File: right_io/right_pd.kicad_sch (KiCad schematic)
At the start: 79 parts, among them J11 USB-C dual-role data/PD port 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, J12 USB-C source-only data port J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, Q2002 2N7002K DFP USB2 enable inver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, U1760 TPS2553DDBVR 1.3A USB branch, U1761 TPS25810RVCR Type-C DFP contr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, U1763 TPD1S514-1YZR 5.9V VBUS OVP, U1765 TPD4E05U06 USB2/CC ESD, U2011 TPD4S201 CC and USB2 short-to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, U2012 CAT24C256 32KB private TPS257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, U2013 TS3USB30E DFP-qualified USB2 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, U2014 SN74LVC2G07 partial-power-dow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, U2015 TVS2200 22V USB VBUS surge cl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, U2016 SN74LVC1G08 DFP and attached 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, U2404 TPS22992SRXNR J11 PP5V gate, U2409 SN74LVC1G08DBVR J12 source pe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, U42 TPS25751AD USB-PD DRP control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, U721 TPS26630RGER PD2 default-off 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

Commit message: rework the board placement and fix more power stuff
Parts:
- added C2631: 100n 50V inverter bypass, Capacitor_SMD:C_0603_1608Metric, symbol Device:C
- added C2681: 100n 50V qualifier bypass, Capacitor_SMD:C_0603_1608Metric, symbol Device:C
- added Q2631: BSS138 switched discharge, Package_TO_SOT_SMD:SOT-23, symbol Q_NMOS_SOT23_GSD:Q_NMOS_SOT23_GSD
- added U2631: SN74LVC1G04DBVR discharge control, Package_TO_SOT_SMD:SOT-23-5, symbol 74xGxx:74LVC1G04
- C2090: value 100n 50V eFuse input local -> 100n 50V input local
- C2091: value 10u 25V eFuse output -> 10u 25V output
- C2092: value 22n eFuse dVdT -> 10n 50V C0G slew control; footprint Capacitor_SMD:C_0402_1005Metric -> Capacitor_SMD:C_0603_1608Metric; MPN GRM155R71H223KA12D -> GRM1885C1H103JA01D
- R2090: value 8.87k 0.02% 5ppm 15/20V eFuse UV/OV top -> 1k 1W switched input discharge; footprint Resistor_SMD:R_0603_1608Metric -> Resistor_SMD:R_2512_6332Metric; MPN TNPU06038K87HZEN00 -> RC2512FR-071KL; Manufacturer Vishay -> Yageo
- R2091: value 562R 0.02% 5ppm 15/20V eFuse UV/OV middle -> 100k discharge gate default-low; MPN TNPU0603562RHZEN00 -> RC0603FR-07100KL; Manufacturer Vishay -> Yageo
- R2092: value 511R 0.02% 5ppm 15/20V eFuse UV/OV bottom -> 1k IMON load; MPN TNPU0603511RHZEN00 -> RC0603FR-071KL; Manufacturer Vishay -> Yageo
- R2093: value 6.04k 1% eFuse 2.98A ILIM -> 267R 0.1% sink breaker; 5.58A nominal; MPN RC0603FR-076K04L -> RT0603BRD07267RL
- R2094: value 47k eFuse default-off pulldown -> 47k sink enable default-off
- R2095: value 10k path-enable series -> 10k sink enable series
- R2096: value 10k eFuse FLT pull-up -> 150k sink PG pull-up; valid with input off; MPN RC0603FR-0710KL -> RC0603FR-07150KL
- U42: PortPolicy DRP;HOST_DATA_ONLY;5_9_15_20V_3A_SINK;5V_900MA_SOURCE;DEFAU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 -> DRP;HOST_DATA_ONLY;5_9_15V_3A_20V_5A_SINK;5V_900MA_SOURCE;D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
- U721: value TPS26630RGER PD2 default-off 3A sink eFuse -> TPS259827ONRGER PD2 sink breaker; footprint Package_DFN_QFN:Texas_RGE0024H_VQFN-24-1EP_4x4mm_P0.5mm_EP2.7x2.7mm_ThermalVias -> ducktop2:Texas_RGE0024M_QFN24_4x4_2EP; symbol Power_Management:TPS26630RGE -> TPS25982:TPS25982; MPN TPS26630RGER -> TPS259827ONRGER; SafetyState MODE_GND_AUTORETRY;PGTH_GND_PGOOD_UNUSED;SHDN_47K_PULLDOWN -> (none)
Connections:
- net GND: now also R2091.2, U721.10 (RETRY_DLY), U721.12 (LDSTRT), U721.14 (GND), U721.26 (GND), U721.4 (GND), U721.5 (GND), C2631.2, C2681.2, Q2631.2 (S), U2631.3 (GND); no longer U721.15 (PGTH), U721.25 (GND), U721.8 (GND)
- net MCU_3V3: now also C2631.1, U2631.5 (VCC)
- net PD2_EFUSE_DVDT: now also U721.15 (dVdt); no longer U721.9 (dVdT)
- net PD2_EFUSE_ILIM: now also U721.8 (ILIM); no longer U721.10 (ILIM)
- net PD2_EFUSE_SHDN: now also U721.6 (EN/UVLO); no longer U721.12 (~{SHDN})
- net PD2_PATH_EN: now also U2631.2
- net PD2_PPHV: now also U721.16 (IN), U721.25 (IN), U721.3 (IN); no longer R2090.1, U721.5 (IN_SYS)
- net PD2_VBUS_GATED: now also R2090.1, U721.19 (OUT), U721.20 (OUT), U721.21 (OUT), U721.22 (OUT), U721.23 (OUT), U721.24 (OUT)
- net SYS_3V3: now also C2681.1
- net PD2_EFUSE_PG: now reaches U721.13 (PG)
- net PD2_EFUSE_PG: now also R2096.2
- removed net PD2_EFUSE_FAULT_N: R2096.2, U721.14 (~{FLT})
- removed net PD2_EFUSE_OV: R2091.2, R2092.1, U721.7 (OVP)
- removed net PD2_EFUSE_UV: R2090.2, R2091.1, U721.6 (UVLO)
- new net PD2_DISCHARGE: Q2631.1 (G), R2091.1, U2631.4
- new net PD2_DISCHARGE_DRAIN: Q2631.3 (D), R2090.2
- new net PD2_EFUSE_IMON: R2092.1, U721.9 (IMON)
- no-connect marks 44 -> 36

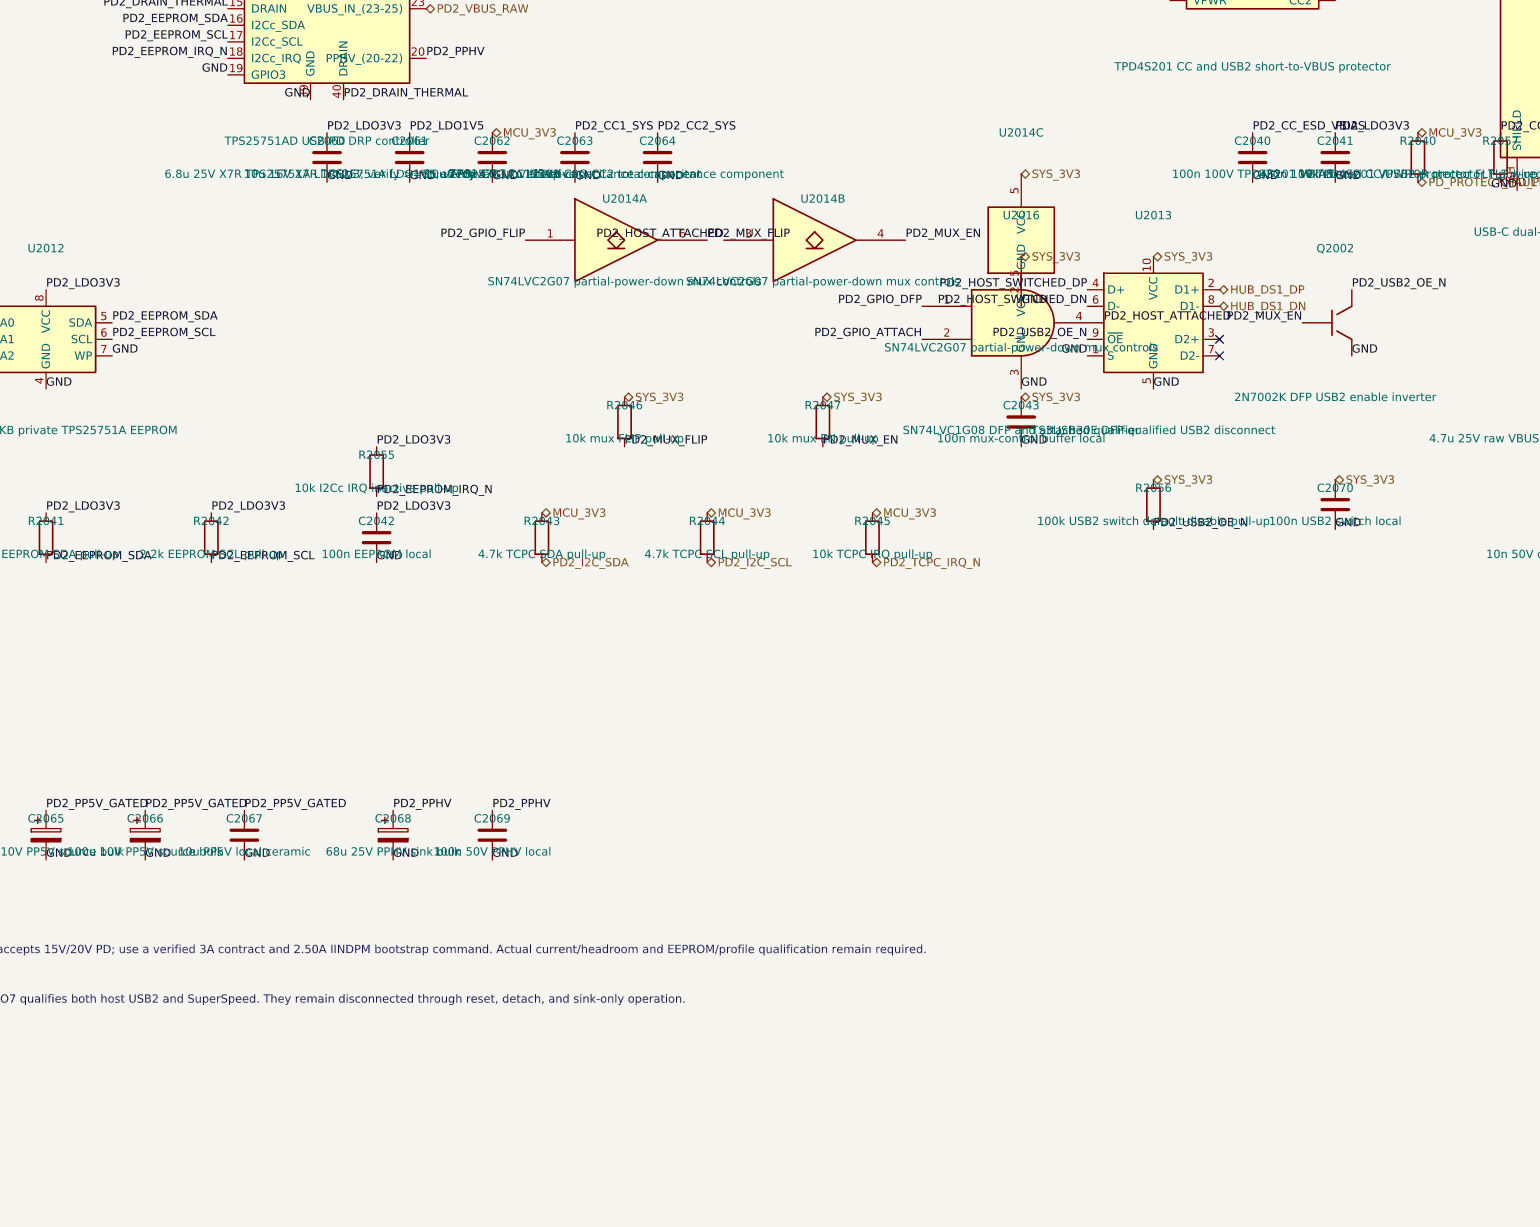
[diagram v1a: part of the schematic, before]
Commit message: sort out the main-board power placement and usb footprints
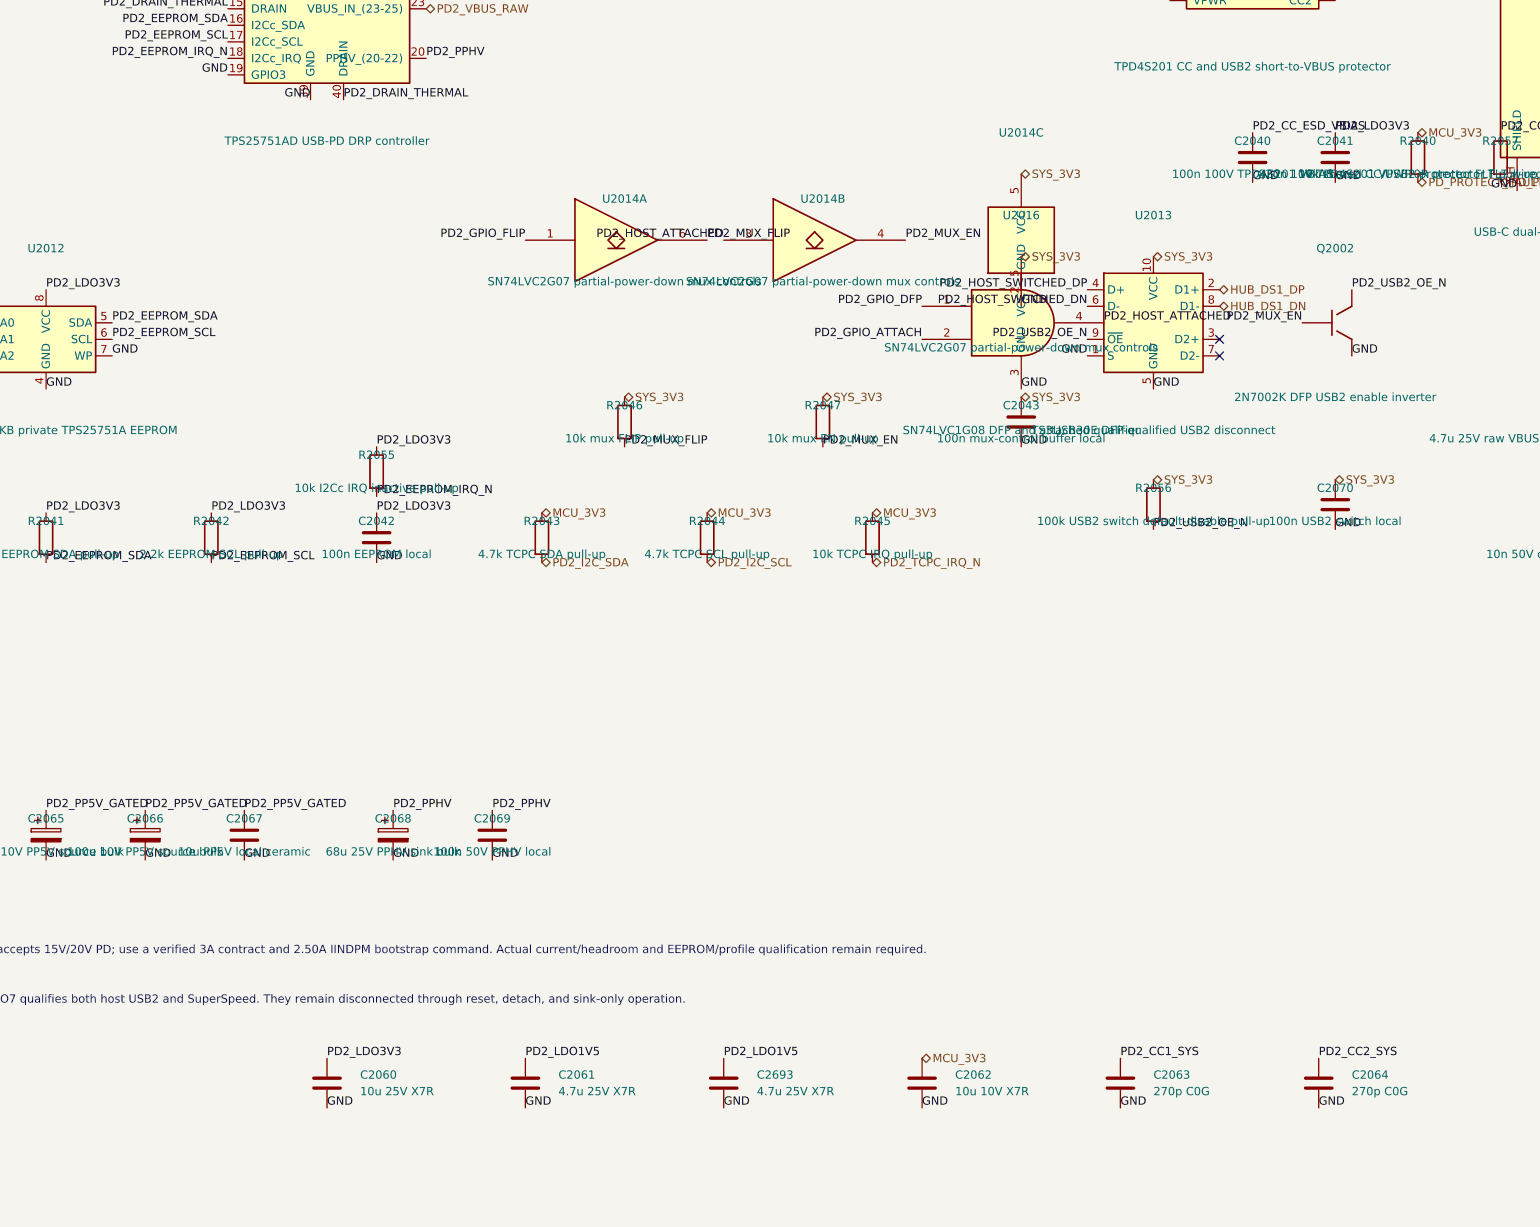
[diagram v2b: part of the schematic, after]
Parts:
- added C2693: 4.7u 25V X7R, Capacitor_SMD:C_1206_3216Metric, symbol Device:C
- C2060: value 6.8u 25V X7R TPS25751A LDO3V3; verify >=5u effective -> 10u 25V X7R; MPN GRM31CR71E685KA88L -> GRM31CR71E106KA12L
- C2061: value 10u 16V X7R TPS25751A LDO1V5; verify 4.5-12u effective -> 4.7u 25V X7R; MPN GRM31CR71C106KA01L -> GRM31CR71E475KA88L
- C2062: value 10u TPS25751A VIN3V3 -> 10u 10V X7R
- C2063: value 270p C0G CC1 total-capacitance component -> 270p C0G
- C2064: value 270p C0G CC2 total-capacitance component -> 270p C0G
- U1763: footprint ducktop2:Texas_TPD1S514_YZ_WCSP-12_1.99x1.29mm_P0.5mm -> ducktop2:Texas_TPD1S514_YZ0012_1.99x1.29mm_P0.4mm
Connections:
- net GND: now also C2693.2
- net PD2_LDO1V5: now also C2693.1
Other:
- moved on the sheet: C2060, C2061, C2062, C2063, C2064
